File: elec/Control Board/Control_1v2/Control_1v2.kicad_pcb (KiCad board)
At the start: 2 copper layers, 205 x 190 mm, 349 parts, among them J1 DB9_Female_MountingHoles, J10 Conn_02x12_Odd_Even, J11 Con_01x02_2.5mm, J12 Con_01x02_2.5mm, J13 Con_01x02_2.5mm, J14 Conn_01x10, J15 DB25_Female_MountingHoles, J16 Conn_01x04, J17 Conn_01x05, J18 Conn_01x04, J19 Conn_01x07, J2 Conn_01x08, J20 Conn_01x04_KK-254_0470531000, J201 Con_01x02_2.5mm, J23 0.100_2Pin, J24 Conn_01x04, J25 Con_01x02_2.5mm, J26 Conn_01x10, J27 Conn_02x12_Odd_Even, J28 Con_01x02_2.5mm, J29 Conn_01x10, J3 Conn_01x08, J30 Con_01x02_2.5mm, J31 Con_01x02_2.5mm, J32 Con_01x02_2.5mm, J33 Con_01x02_2.5mm, J34 Con_01x02_2.5mm, J35 Conn_02x05_Odd_Even, J36 Conn_02x05_Odd_Even, J37 Conn_01x04, J38 Conn_02x06_Odd_Even, J39 Conn_02x06_Odd_Even, J4 Conn_01x08, J40 Conn_02x06_Odd_Even, J41 Conn_02x06_Odd_Even, J42 Conn_02x06_Odd_Even, J43 Conn_01x30, J44 Conn_01x30, J45 Conn_01x30, J46 Conn_01x30, J47 Conn_01x30, J48 Conn_01x30, J49 Conn_01x30, J5 Conn_01x08, J50 Conn_01x30, J51 Conn_01x30, J52 Conn_01x30, J53 Conn_01x30, J54 Conn_01x30, J55 Conn_02x06_Odd_Even, J56 Conn_02x06_Odd_Even, J57 Conn_02x06_Odd_Even, J58 Conn_02x06_Odd_Even, J59 Conn_02x06_Odd_Even, J6 Conn_01x08, J7 Conn_01x10, J8 Conn_02x18_Odd_Even, J801 Conn_01x03_0.1", J802 Con_01x02_0.1", J803 Screw_Terminal_01x04_5.08mm, J804 Screw_Terminal_01x02_5.08mm, J805 Con_01x02_0.1", J9 Conn_01x10, K801 Relay SRU-12VDC, Q1 BSS138, Q10 BSS138, Q11 BSS138, Q12 BSS138, Q13 BSS138, Q14 BSS138, Q2 NCE01P30K, Q3 BSS138, Q4 BSS138, Q801 BSS138, Q9 BSS138

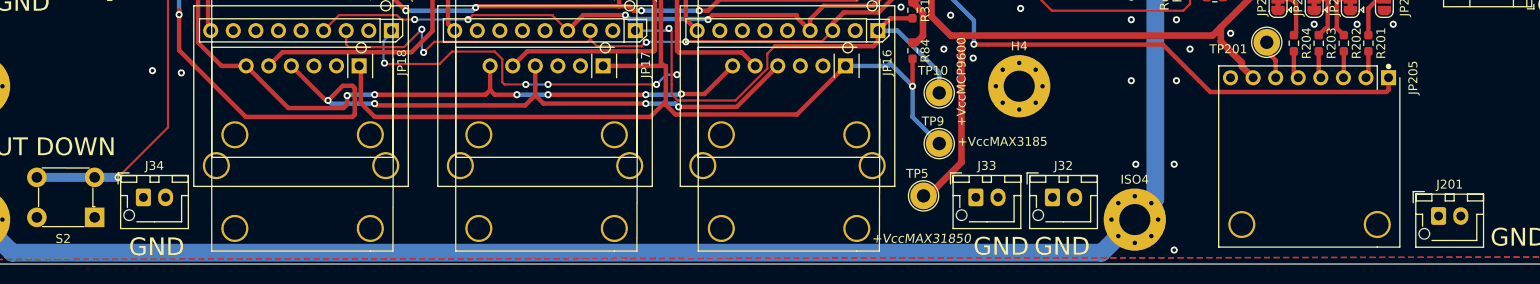
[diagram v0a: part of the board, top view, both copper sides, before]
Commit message: Add a connector next to the SHUTDOWN switch. Add 3D file for relay.
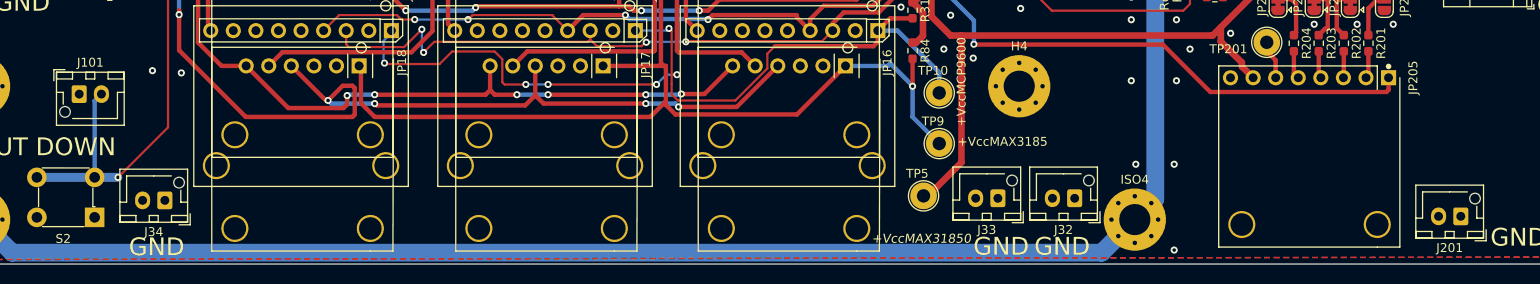
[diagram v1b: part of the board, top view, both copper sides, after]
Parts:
- added J101: Con_01x02_2.5mm, PubInv_KiCad_PCB:JST_XH_B2B-XH-AM_1x02_P2.50mm_Vertical, F.Cu at (66.3, 205.9)
- J23: value 0.100_2Pin -> Con_01x02_0.1"
- moved J32 2.50 mm to (178.2, 217.6), turned to 180 degrees
- moved J201 2.50 mm to (221.7, 219.6), turned to 180 degrees
- moved J33 2.48 mm to (169.6, 217.6), turned to 180 degrees
- moved J34 2.44 mm to (75.9, 217.8), turned to 180 degrees
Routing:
- net SHUTDOWN: track 132.4 -> 142.1 mm
